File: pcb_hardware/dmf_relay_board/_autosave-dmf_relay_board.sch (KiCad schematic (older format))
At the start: 69 parts, among them J1 HVPS, J2 Relays to Electrodes 1, J3 Relays to Electrodes 2, J4 Electrodes from Relay 1, J5 Electrodes from Relay 2, U1 HV507

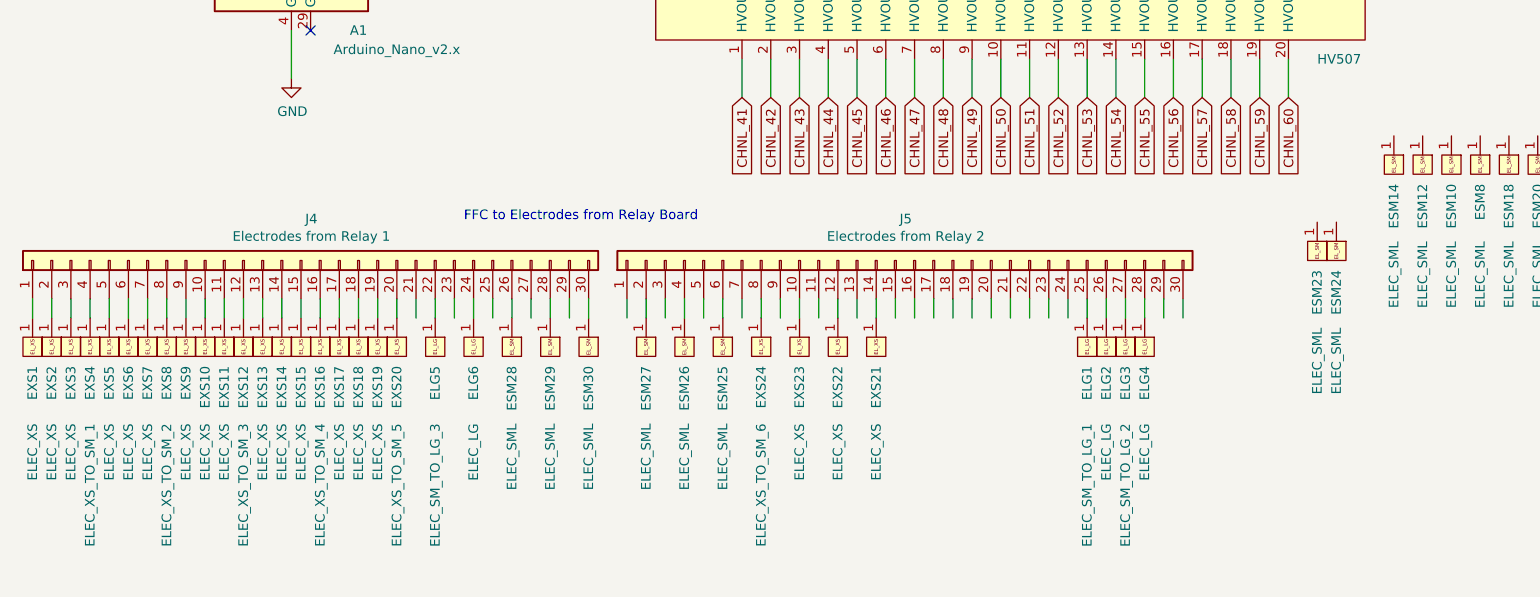
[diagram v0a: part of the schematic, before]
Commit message: electrode footprints placed - routing now
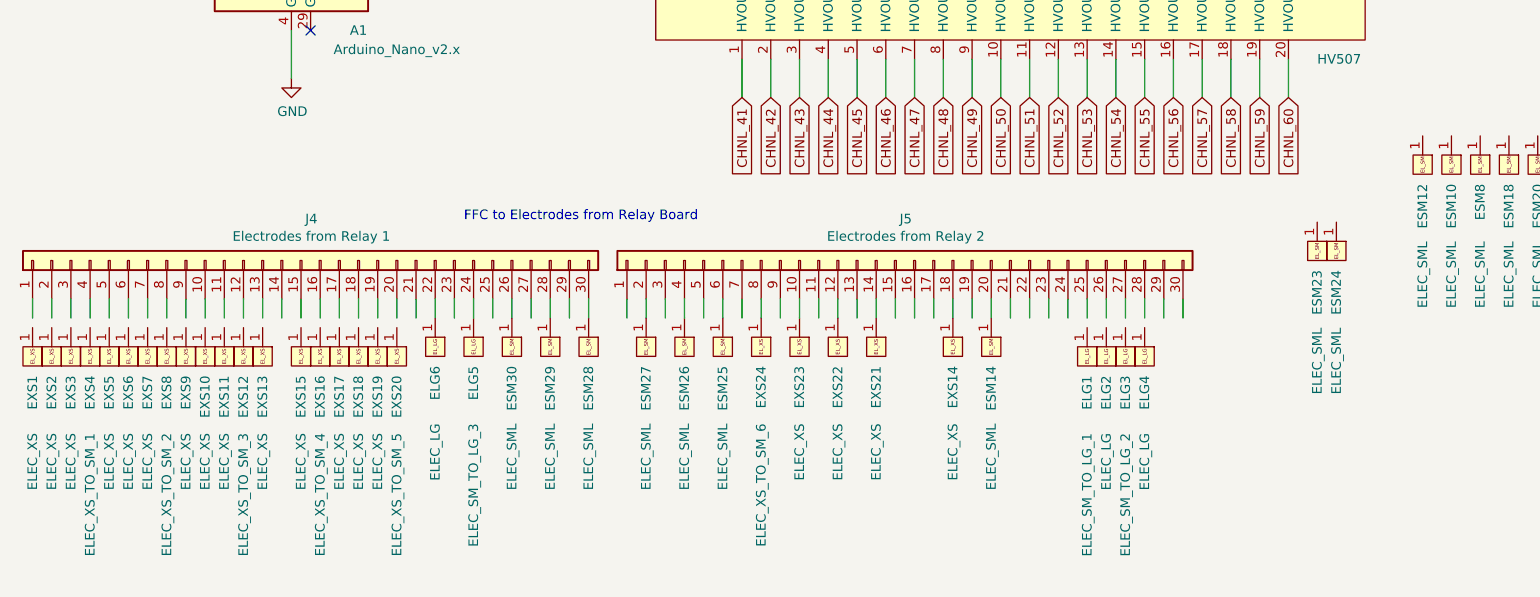
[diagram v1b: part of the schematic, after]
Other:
- moved on the sheet: ELG1, ELG2, ELG3, ELG4, ELG5, ELG6, ESM14, ESM28, ESM30, EXS1, EXS10, EXS11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

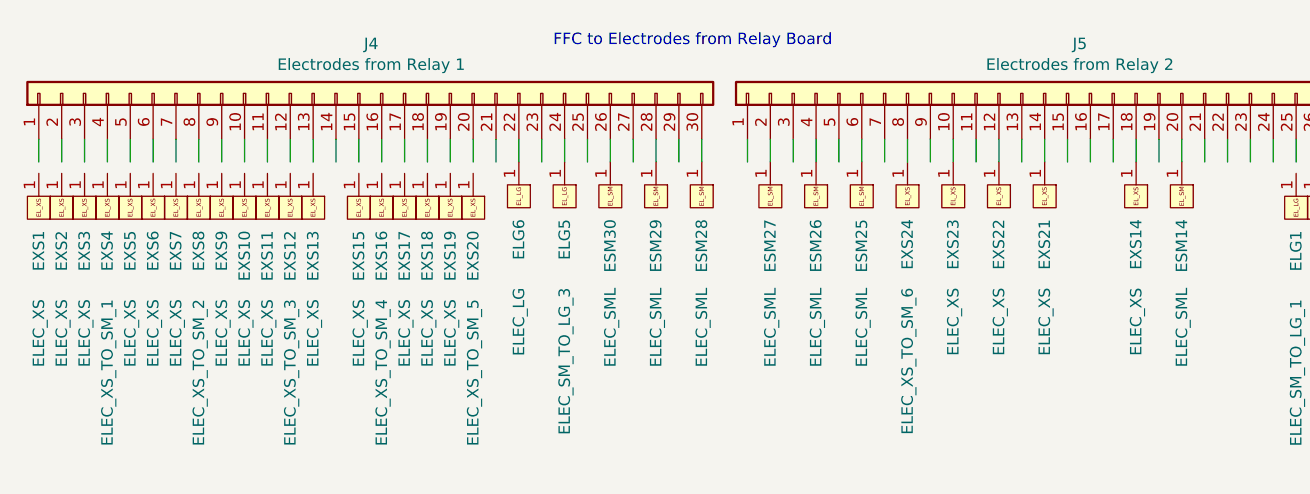
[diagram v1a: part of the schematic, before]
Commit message: electrode pads fixed for routing
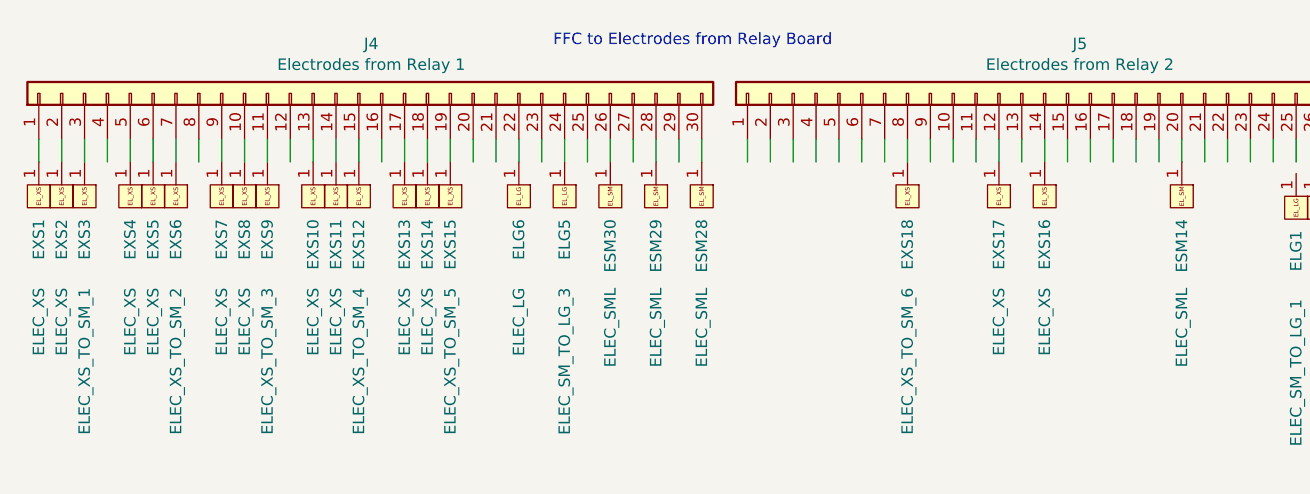
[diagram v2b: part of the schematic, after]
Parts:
- removed ESM25, ESM26, ESM27: ELEC_SML, dmf_relay_board:ELECTRODE_2_75_4MIL_4_5, symbol dmf_relay_board:ELEC_SML
- removed EXS11, EXS14, EXS19, EXS23, EXS3, EXS7: ELEC_XS, dmf_relay_board:ELECTRODE_1_375_4MIL_4_5, symbol dmf_relay_board:ELEC_XS
- renumbered EXS13 to EXS10, EXS15 to EXS11, EXS16 to EXS12, EXS17 to EXS13, EXS18 to EXS14, EXS20 to EXS15, EXS21 to EXS16, EXS22 to EXS17, EXS24 to EXS18, EXS4 to EXS3, EXS5 to EXS4, EXS6 to EXS5, EXS8 to EXS6, EXS9 to EXS7, EXS10 to EXS8, EXS12 to EXS9
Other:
- moved on the sheet: EXS1, EXS10, EXS11, EXS12, EXS13, EXS14, EXS15, EXS2, EXS3, EXS4, EXS5, EXS6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
